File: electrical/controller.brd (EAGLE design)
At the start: 101.6 x 25.4 mm, 36 parts, among them IC1 MCP6232, IC2 LTC1661MSOP8, IC3 MCP6232, IC4 ICM7555, IC5 CD40109B, J3 455-1750-1-ND, Q1 DMP3098, Q3 600mA/40V, U1 U3V16F15, U2 U3V16F15

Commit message: Slight update to switch footprint
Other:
- board text removed: "ALL RESISTORS 10k UNLESS OTHERWISE NOTED"
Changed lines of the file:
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@@
 <text x="39.37" y="23.622" size="0.762" layer="25" font="vector" ratio="18">RESET</text>
 <text x="65.024" y="16.51" size="0.762" layer="25" font="vector" ratio="18">BAT  OFF  USB</text>
-<text x="13.208" y="1.016" size="0.762" layer="25" font="vector" ratio="18">ALL RESISTORS 10k
-UNLESS OTHERWISE NOTED</text>
 <text x="54.102" y="10.414" size="1.27" layer="26" font="vector" ratio="18" rot="MR0">Douglas Hutchings
 Double Pendulum Driver
@@
 <contactref element="J1" pad="VBUS2"/>
 <contactref element="S_PWR" pad="P3"/>
+<wire x1="60.997" y1="18.628" x2="68.199" y2="21.336" width="0" layer="19" extent="1-1"/>
+<wire x1="56.097" y1="18.628" x2="60.997" y2="18.628" width="0" layer="19" extent="1-1"/>
 </signal>
 <signal name="USR3">

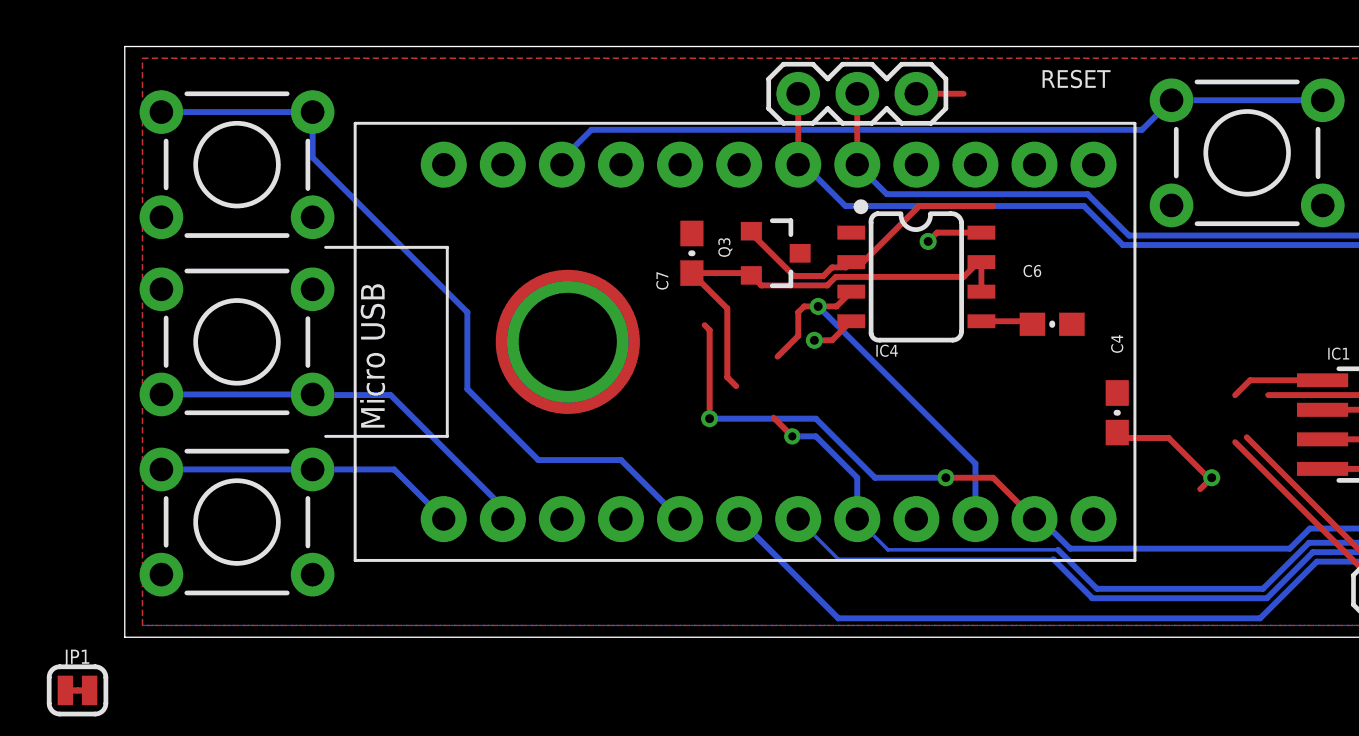
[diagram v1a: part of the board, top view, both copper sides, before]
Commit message: Change arduino footprint
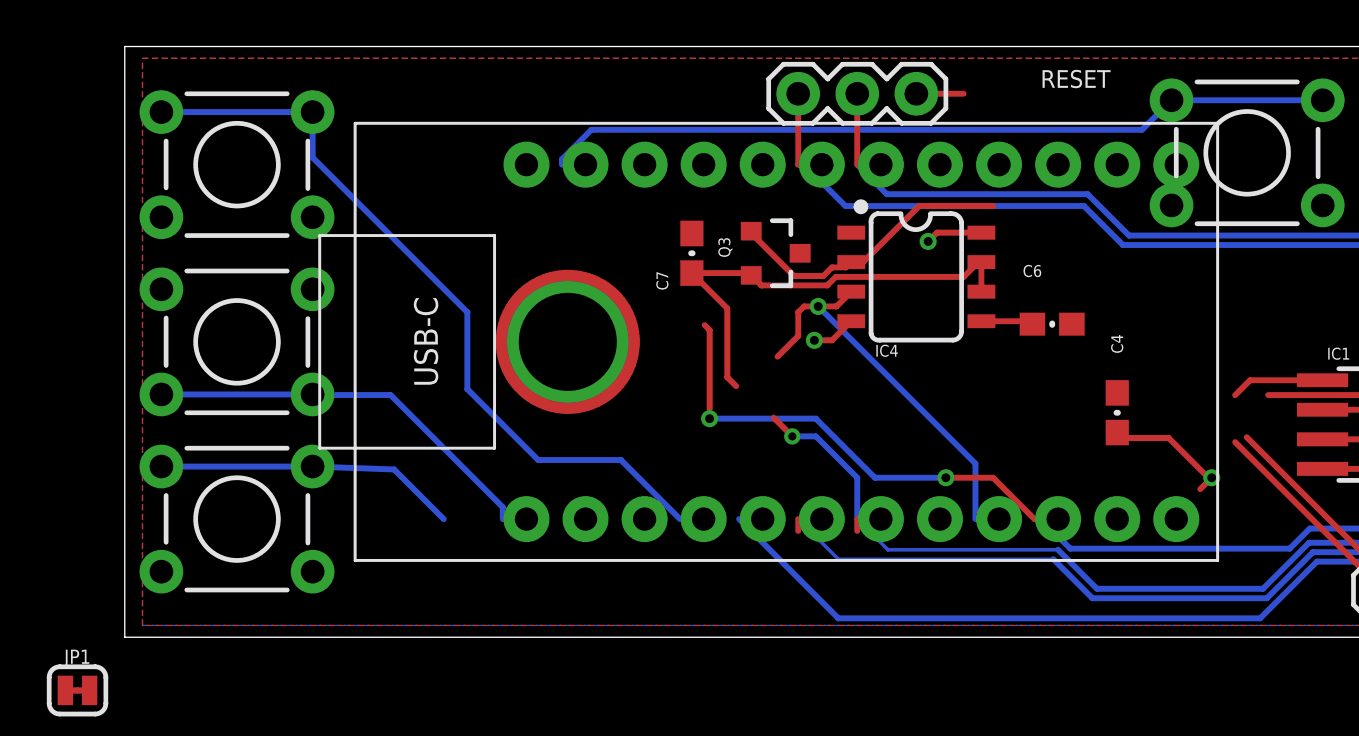
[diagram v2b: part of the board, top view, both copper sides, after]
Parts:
- UC1: device BEST_Custom:ARDUINO_PRO_MICRO_2D -> BEST_Custom:ARDUINO_PRO_MICRO_USBC
- moved UC1 15.4 mm to (31.2, 12.7)
- moved S1 0.13 mm to (4.83, 5.08)

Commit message: Plop some things onto the PCB, lots of work to do.
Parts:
- moved IC5 118.7 mm to (87.1, 6.10), turned to 90 degrees
- moved JP1 100.7 mm to (97.3, 14.2), turned to 180 degrees
- moved R4 99.8 mm to (82.5, 3.56), turned to 90 degrees
- moved JP2 95.6 mm to (83.3, 10.7), turned to 90 degrees
- moved R6 92.3 mm to (65.3, 10.9), turned to 90 degrees
- moved IC2 88.2 mm to (45.2, 16.5)
- moved R5 86.6 mm to (63.2, 15.5), turned to 180 degrees
- moved S4 5.14 mm to (53.3, 20.1), turned to 270 degrees
- moved J1 5.08 mm to (63.6, 18.3)
- moved S_PWR 3.39 mm to (76.2, 20.6)
- moved C2 1.91 mm to (70.0, 7.11)
- moved C4 1.91 mm to (44.6, 9.65)
- moved C6 1.91 mm to (41.8, 13.5)
- moved C7 1.91 mm to (26.3, 16.5)
- moved D1 1.91 mm to (74.8, 8.13)
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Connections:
- removed net 12V: IC5.16, JP1.1
- net 15V: now also IC5.16, JP1.1
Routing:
- net COIL: track 35.6 -> 24.9 mm
- net DRIVE: track 67.6 -> 58.5 mm, vias 3 -> 0
- net 15V: track 26.1 -> 34.6 mm, vias 4 -> 8
- net N$1: track 0.00 -> 8.29 mm
- net N$4: track 11.4 -> 4.66 mm
- net N$7: track 20.2 -> 14.5 mm
- net PEAK_RST: track 58.2 -> 53.4 mm, vias 2 -> 0
- net RST: track 34.0 -> 38.6 mm
- net N$2: track 0.00 -> 3.39 mm
- net TIMER_RESTART: track 16.9 -> 13.6 mm
- net N$9: track 0.00 -> 3.09 mm
- net N$8: track 0.00 -> 2.65 mm
- net GND: track 17.9 -> 20.1 mm
- net TIMER_RST: track 14.5 -> 12.5 mm
- net USR2: track 17.2 -> 19.1 mm
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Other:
- board size 101.6 x 25.4 mm -> 103.5 x 25.4 mm

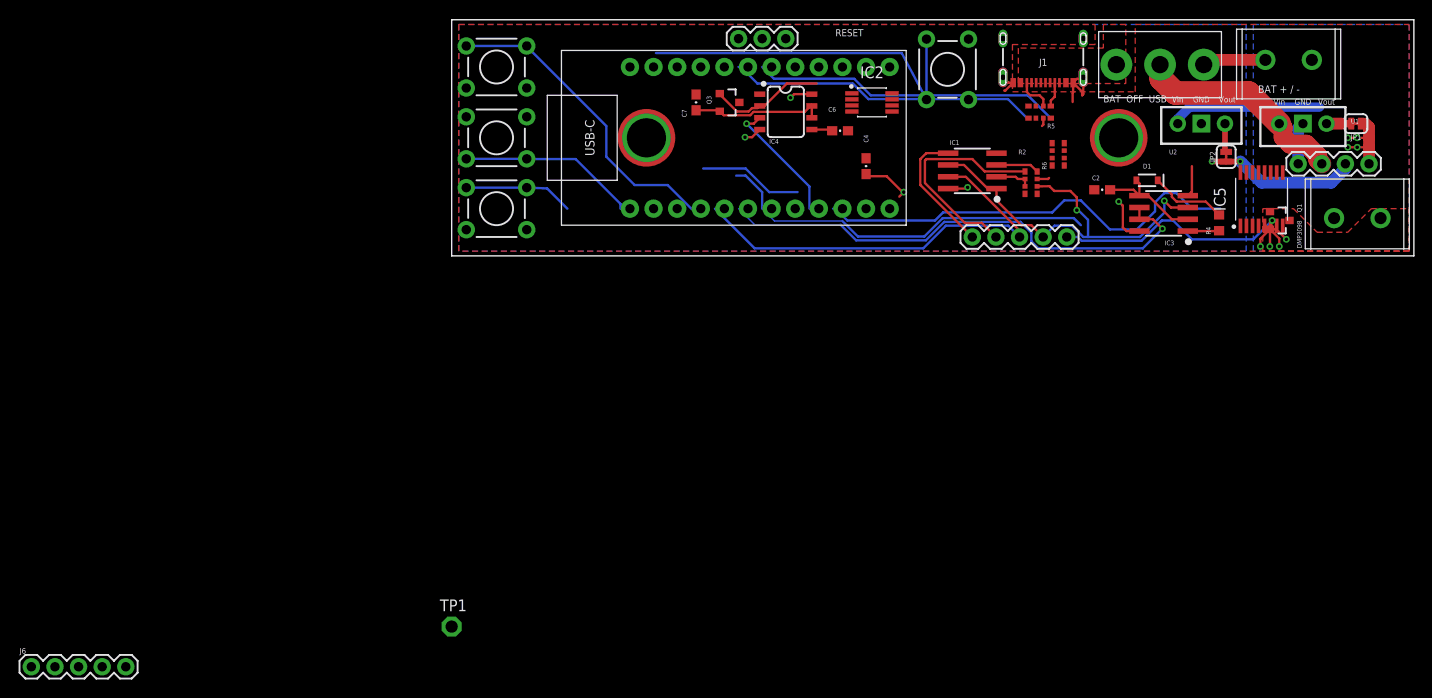
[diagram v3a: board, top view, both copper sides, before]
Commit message: First attempt at routing D3
Now lets put it in Solidworks and check button accessibility.
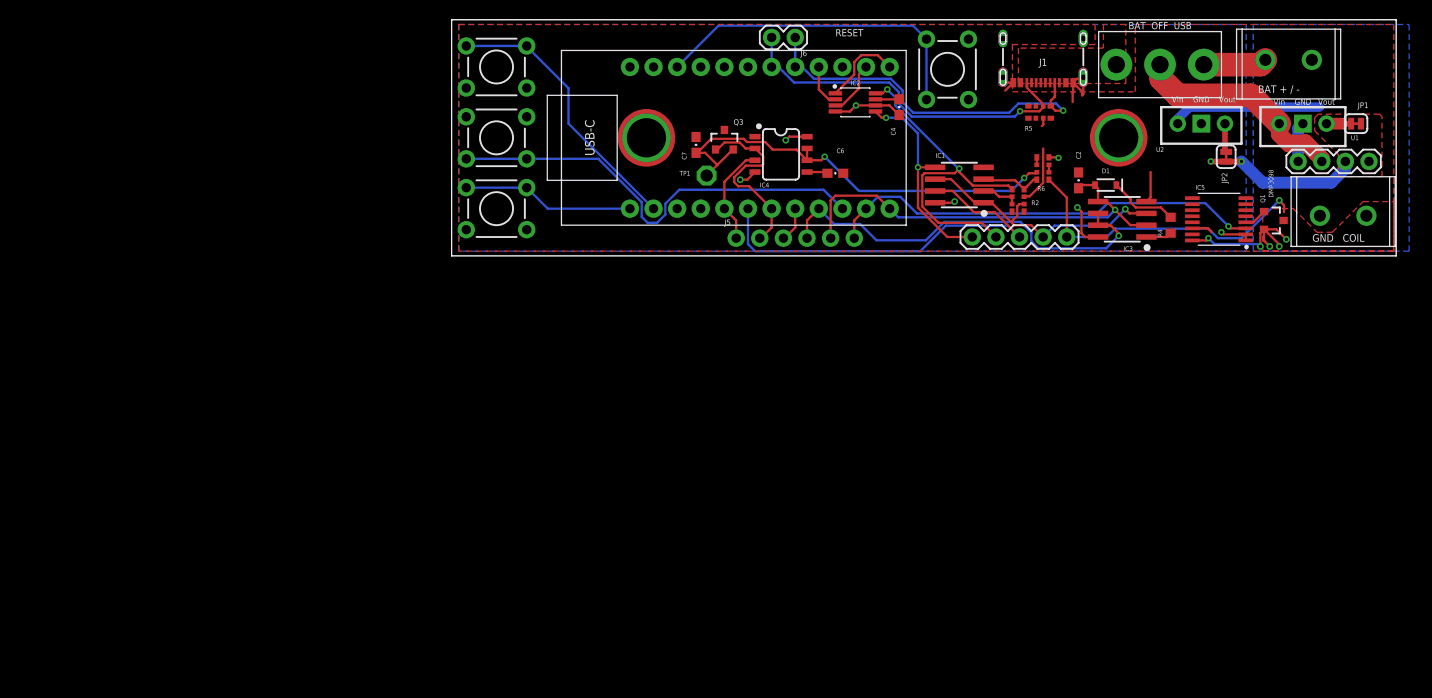
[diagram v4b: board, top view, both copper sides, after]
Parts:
- removed J3: 455-1750-1-ND, SparkFun-Connectors:1X03
- added J5: (no value), SparkFun-Connectors:1X06_NO_SILK
- J6: device SparkFun-Connectors:1X05 -> SparkFun-Connectors:1X02
- moved J6 106.5 mm to (37.0, 23.5), turned to 180 degrees
- moved TP1 55.7 mm to (27.4, 8.64)
- moved C4 7.28 mm to (48.1, 16.0)
- moved R4 5.21 mm to (77.3, 3.30)
- moved IC5 5.06 mm to (82.5, 3.94), turned to 180 degrees
- moved C6 4.60 mm to (41.3, 8.89)
- moved IC4 4.60 mm to (35.4, 10.9)
- moved C7 4.57 mm to (26.3, 11.9)
- moved IC3 4.49 mm to (72.1, 3.94)
- moved D1 4.47 mm to (70.4, 7.62)
- moved Q3 4.10 mm to (29.3, 12.4), turned to 0 degrees
- moved C2 2.74 mm to (67.4, 8.13), turned to 90 degrees
- moved R2 2.36 mm to (61.0, 5.97)
- moved R6 2.25 mm to (63.6, 9.40)
- moved IC1 2.07 mm to (54.6, 7.62)
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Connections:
- net 5V: now also R6.P4; no longer R6.P5
- net A_PEAK: now also J5.4, UC1.6; no longer J6.4, UC1.4
- net CC1: now also J6.1; no longer J3.2
- net CC2: now also J6.2; no longer J3.3
- net DEBUG_WAKE: now also J5.3, UC1.5; no longer J6.5, UC1.9
- net DRIVE: now also J5.6; no longer J6.1
- net N$10: now also R6.P5; no longer R6.P4
- net N$3: now also R6.P2; no longer R6.P7
- net N$7: now also R6.P7; no longer R6.P2
- net PEAK_RST: now also J5.5, UC1.9; no longer J6.3, UC1.5
- net TIMER_RESTART: now also J5.1, UC1.2; no longer J6.2, UC1.7
- net TIMER_RST: now also J5.2, UC1.4; no longer J3.1, UC1.6
- net USR2: now also UC1.7; no longer UC1.RXI
- net USR3: now also UC1.RXI; no longer UC1.2
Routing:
- net N$7: track 14.5 -> 48.7 mm, vias 0 -> 2
- net USR2: track 19.1 -> 47.2 mm
- net SHIFT: track 43.0 -> 29.6 mm, vias 2 -> 1
- net V1: track 23.8 -> 37.0 mm, vias 0 -> 2
- net DRIVE: track 58.5 -> 47.4 mm, vias 0 -> 1
- net A_PEAK: track 54.6 -> 44.6 mm
- net GND: track 20.1 -> 29.4 mm
- net COIL: track 24.9 -> 33.8 mm
- net CS: track 0.00 -> 8.85 mm
- net V2: track 14.0 -> 22.5 mm, vias 0 -> 2
- net TIMER_RST: track 12.5 -> 20.1 mm
- net PEAK_RST: track 53.4 -> 46.3 mm, vias 0 -> 1
- net 5V: track 33.4 -> 40.2 mm, vias 7 -> 9
- net USR1: track 11.8 -> 18.5 mm
- net MOSI: track 0.00 -> 5.92 mm
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- added copper zone on layer 1, net 15V
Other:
- board size 103.5 x 25.4 mm -> 101.6 x 25.4 mm
- board text added: "CC1 CC2"
- board text added: "COIL GND"
- board text added: "DRIVE PEAK_RESET A_PEAK DEBUG_WAKE TIMER_RST TIMER_RESTART"
- board text added: "Douglas Hutchings Double Pendulum Driver Rev D3 8-15-25"
- board text added: "GND COIL"
- board text removed: "DRIVE TIMER_RESTART PEAK_RESET A_PEAK"
- board text removed: "Douglas Hutchings Double Pendulum Driver Rev D2 7-21-25"
- board text removed: "TIMER_RST CC1 CC2"

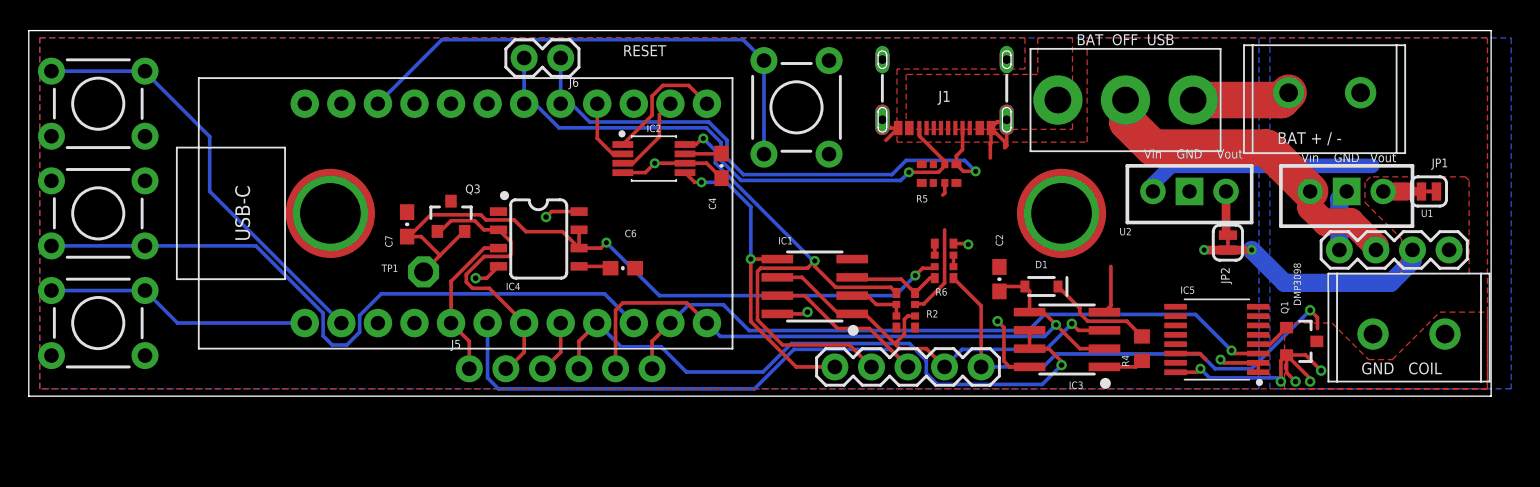
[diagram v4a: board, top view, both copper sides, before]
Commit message: Update routing, silkscreen, in minor ways.
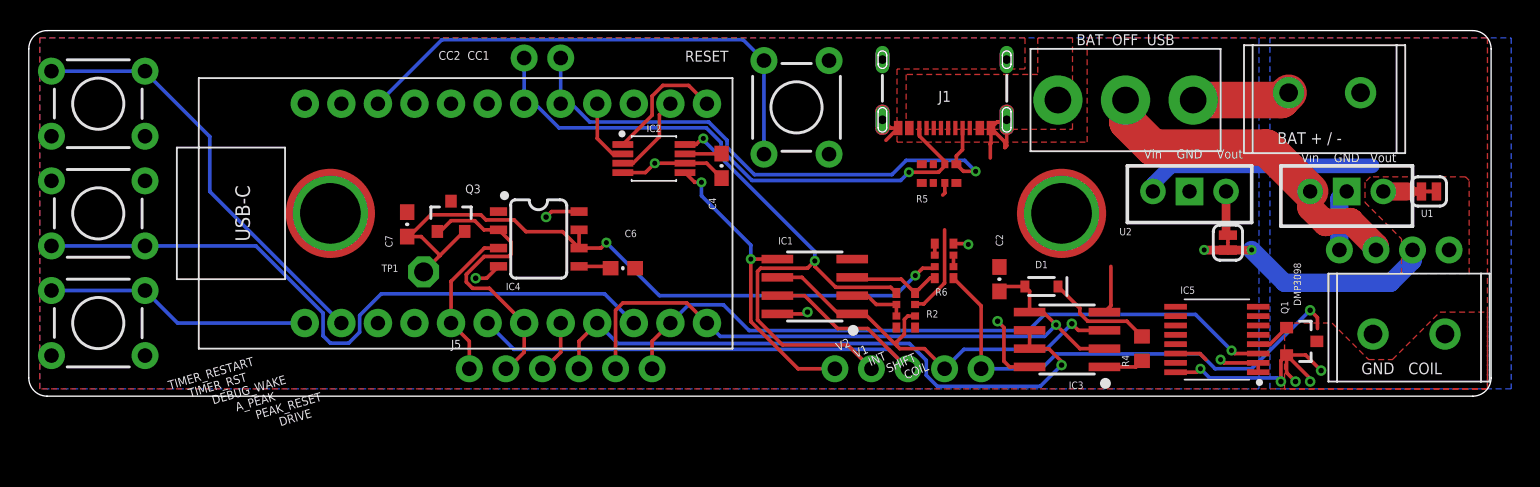
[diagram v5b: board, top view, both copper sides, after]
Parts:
- J2: device SparkFun-Connectors:1X04 -> SparkFun-Connectors:1X04_NO_SILK
- J4: device SparkFun-Connectors:1X05 -> SparkFun-Connectors:1X05_NO_SILK
- J6: device SparkFun-Connectors:1X02 -> SparkFun-Connectors:1X02_NO_SILK
- moved J4 0.13 mm to (56.0, 1.91)
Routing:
- net INT: track 46.1 -> 41.7 mm
- net A_PEAK: track 44.6 -> 43.1 mm
- net V2: track 22.5 -> 21.6 mm
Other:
- outline, holes or cut-outs redrawn
- board text added: "CC2 CC1"
- board text added: "TIMER_RESTART TIMER_RST DEBUG_WAKE A_PEAK PEAK_RESET DRIVE"
- board text added: "V2 V1 INT SHIFT COIL"

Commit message: Tweak positions, final D3 for prod
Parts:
- moved J2 2.03 mm to (89.0, 10.2)
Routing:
- net VIN: track 23.5 -> 21.4 mm
- net 5V: track 40.2 -> 38.5 mm
- net GND: track 29.4 -> 30.2 mm

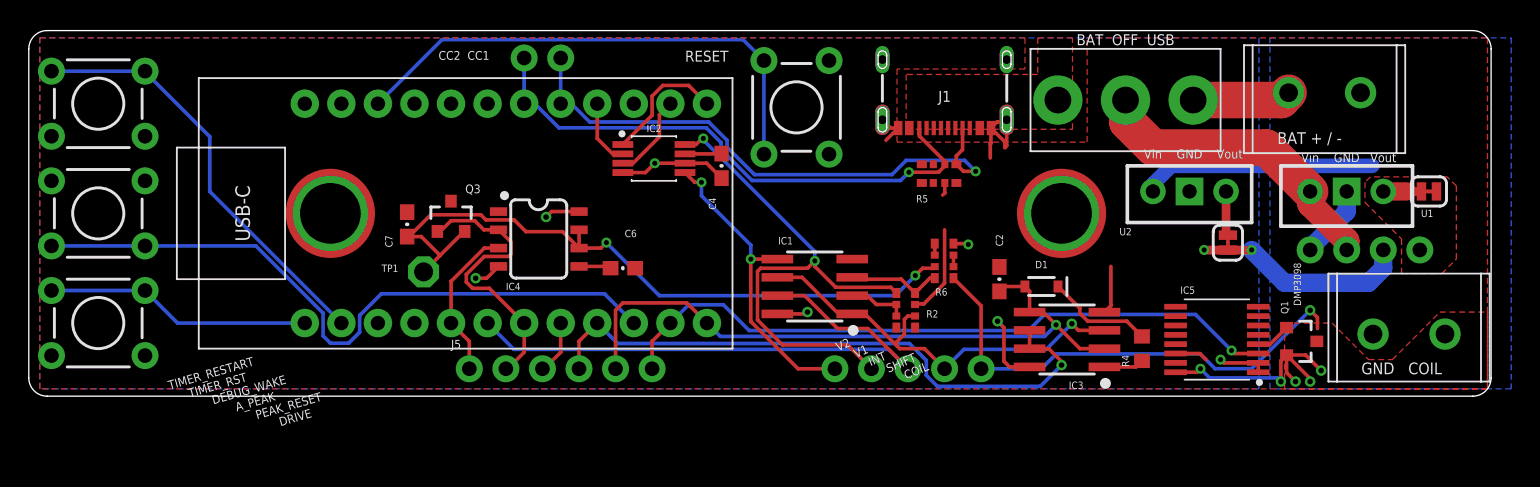
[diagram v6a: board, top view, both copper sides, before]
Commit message: Fix many erratta, overhaul power planes
Rev D4 now WIP.
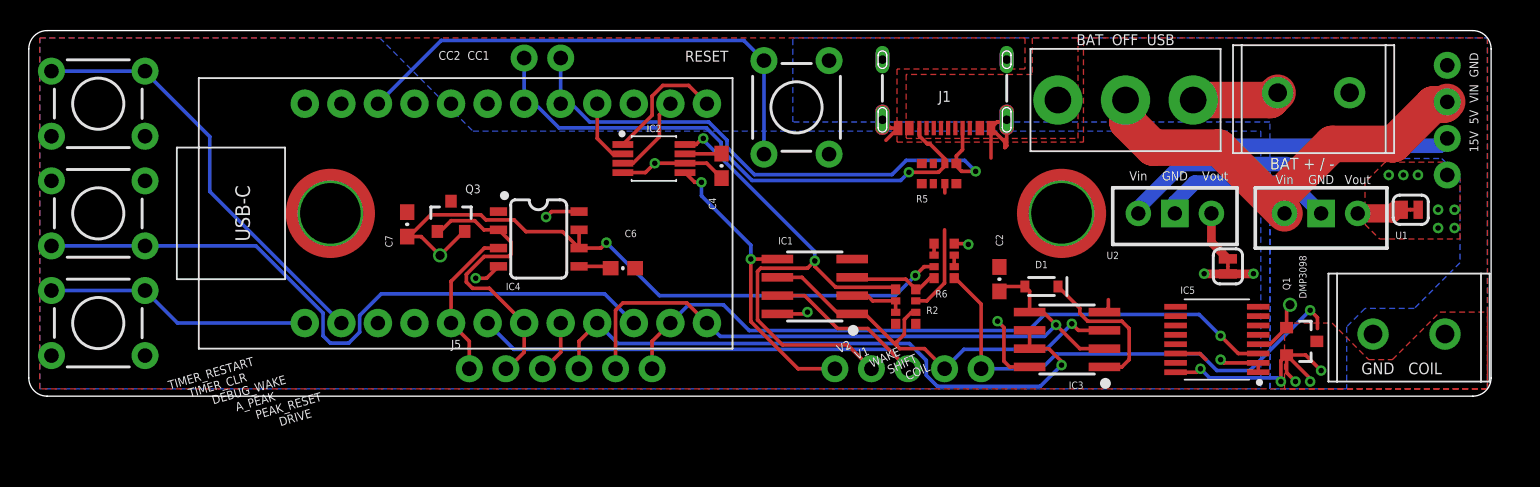
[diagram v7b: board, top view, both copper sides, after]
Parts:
- removed R4: 220, BEST_Custom:R0603
- removed TP1: TPSPAD1-13, testpad:P1-13
- moved J2 16.0 mm to (98.6, 23.0), turned to 270 degrees
- moved U1 2.34 mm to (89.8, 12.7)
- moved U2 1.83 mm to (79.6, 12.7)
- moved JP1 1.80 mm to (96.0, 13.0)
- moved JP2 1.65 mm to (83.3, 9.02)
- moved ST1 0.76 mm to (94.9, 24.4)
- moved R2 0.25 mm to (61.0, 6.22)
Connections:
- net DEBUG_WAKE renamed DEBUG
- net INT renamed WAKE
- net TIMER_RST renamed TIMER_CLR
- removed net N$2: IC3.1, R4.1
- net N$1: now also IC3.1; no longer R4.2
- net N$7: no longer TP1.TP
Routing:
- net VIN: track 21.4 -> 30.5 mm
- net GND: track 30.2 -> 34.7 mm
- net 15V: track 33.5 -> 29.2 mm, vias 5 -> 12
- net 5V: track 38.5 -> 42.5 mm
- net N$1: track 7.47 -> 10.4 mm
- net N$2: track 2.78 -> 0.00 mm
- net N$11: track 2.45 -> 4.13 mm, vias 0 -> 1
- net N$7: track 48.7 -> 47.1 mm, vias 2 -> 3
- net VBAT: track 6.84 -> 6.08 mm
- net N$8: track 2.65 -> 3.27 mm
- net N$9: track 3.09 -> 3.64 mm
- added copper zone on layer 16, net GND
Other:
- board text added: "DRIVE PEAK_RESET A_PEAK DEBUG_WAKE TIMER_CLR TIMER_RESTART"
- board text added: "Douglas Hutchings Double Pendulum Driver Rev D4 12-28-25"
- board text added: "TIMER_RESTART TIMER_CLR DEBUG_WAKE A_PEAK PEAK_RESET DRIVE"
- board text added: "V2 V1 WAKE SHIFT COIL"
- board text removed: "DRIVE PEAK_RESET A_PEAK DEBUG_WAKE TIMER_RST TIMER_RESTART"
- board text removed: "Douglas Hutchings Double Pendulum Driver Rev D3 8-15-25"
- board text removed: "TIMER_RESTART TIMER_RST DEBUG_WAKE A_PEAK PEAK_RESET DRIVE"
- board text removed: "V2 V1 INT SHIFT COIL"
